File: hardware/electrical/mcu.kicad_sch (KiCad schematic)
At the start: 45 parts, among them J2 STDC14, SW1 SW_Push, SW2 SW_SPST, U2 STM32F446ZET6, U3 SRV05-4, Y1 X322516MLB4SI, Y2 Q13FC1350000400

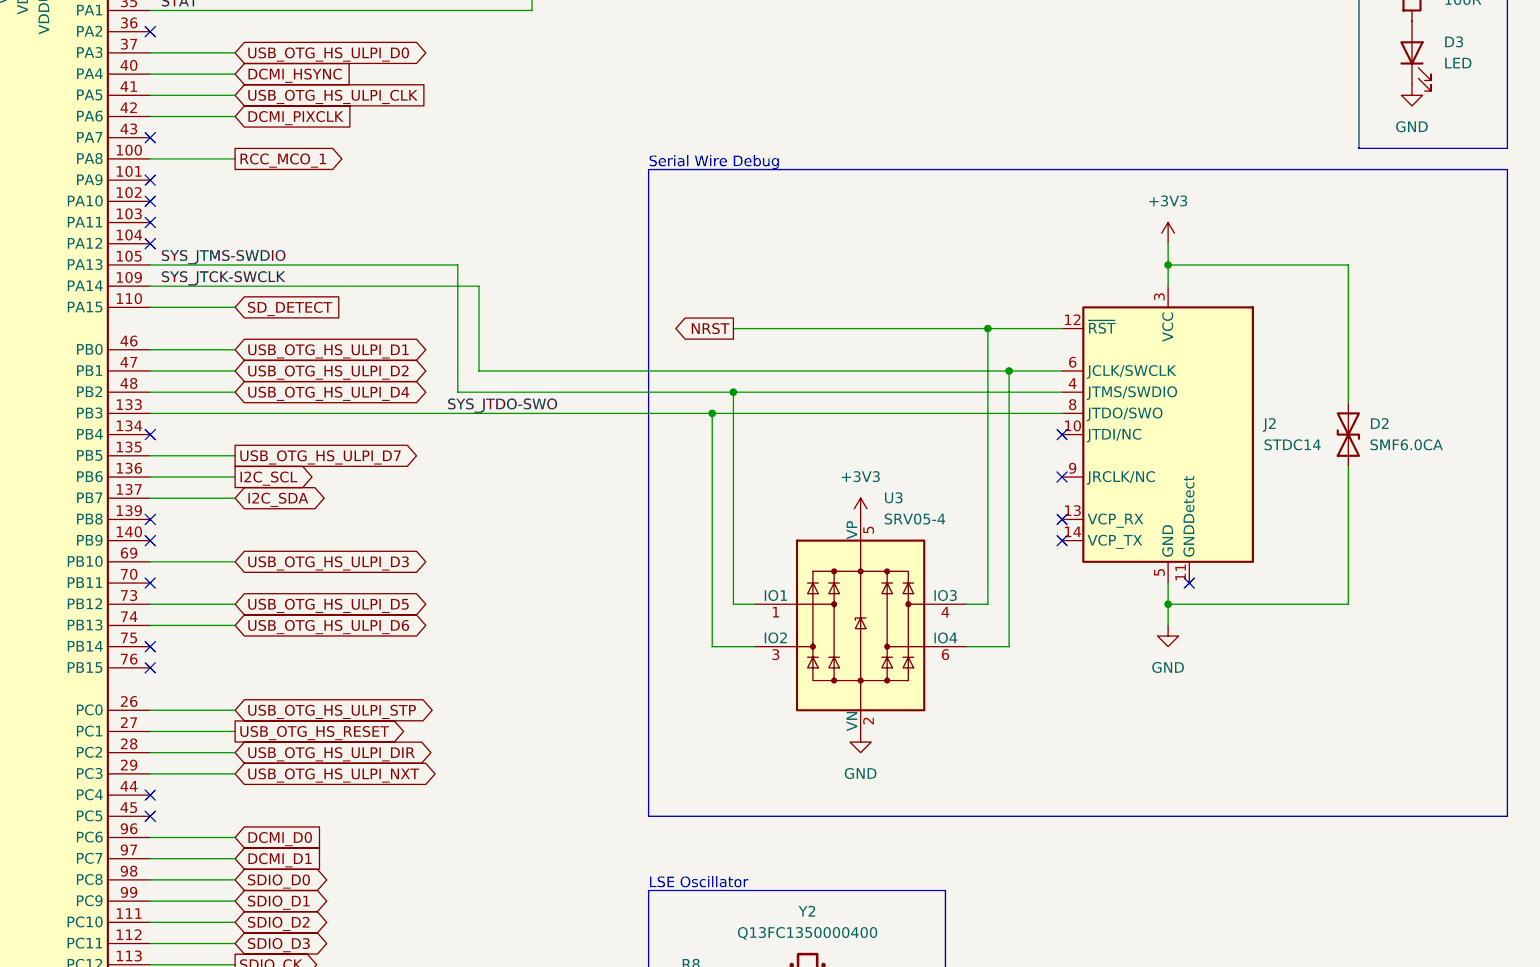
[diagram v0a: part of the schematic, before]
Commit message: Remove ESD protection from SWD connector
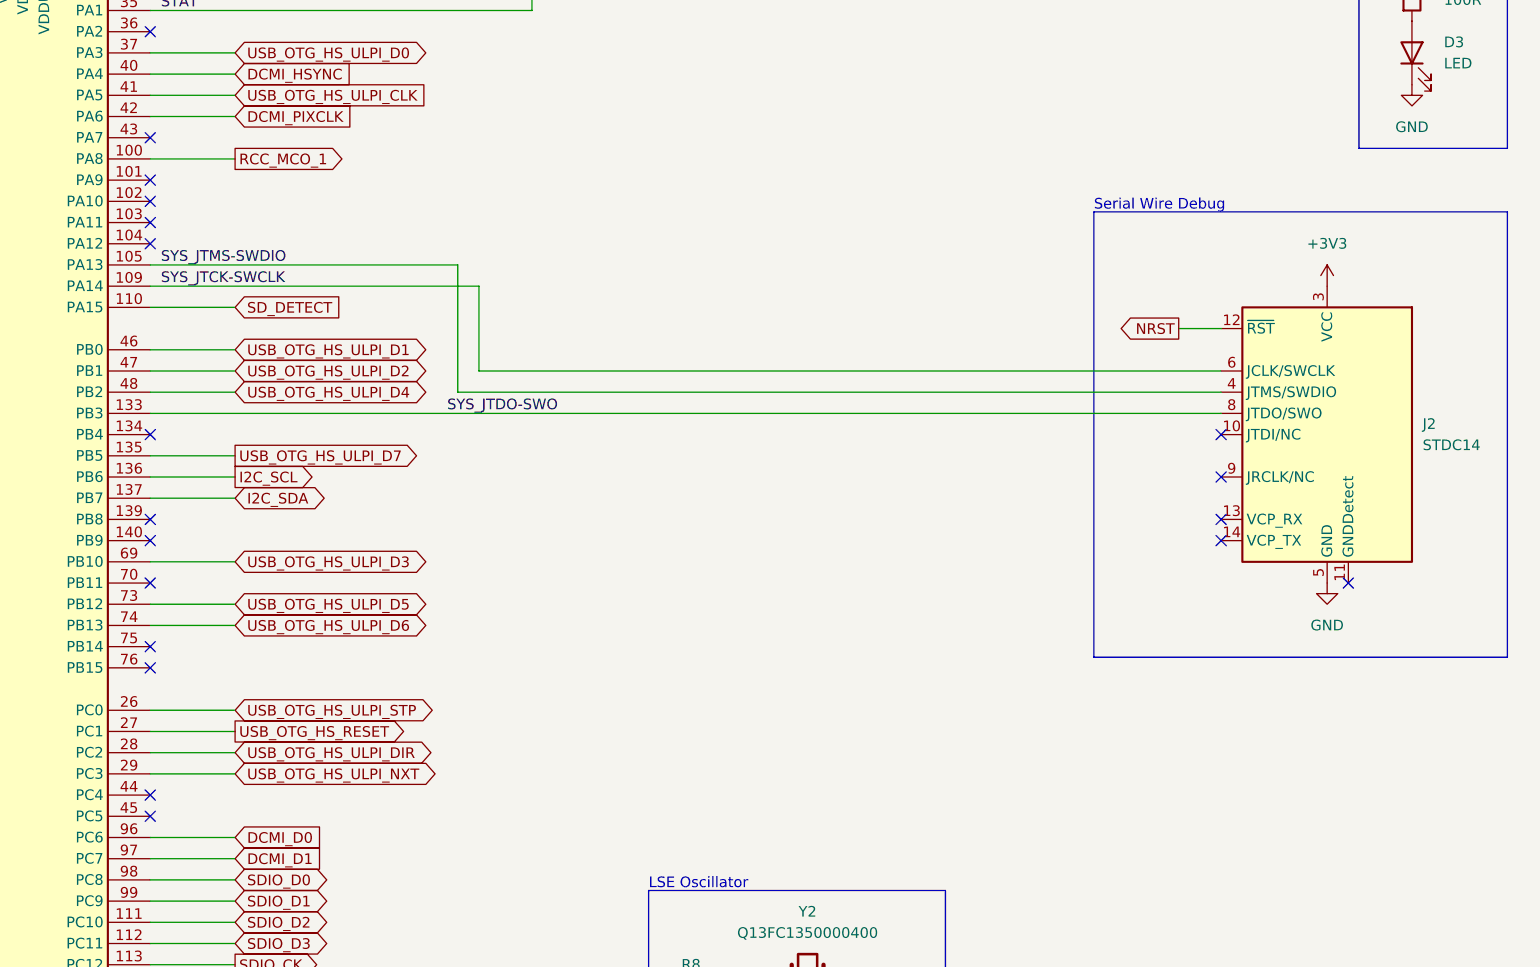
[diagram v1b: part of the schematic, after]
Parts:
- removed D2: SMF6.0CA, symbol Device:D_TVS
- removed U3: SRV05-4, Package_TO_SOT_SMD:SOT-23-6, symbol Power_Protection:SRV05-4
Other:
- moved on the sheet: J2

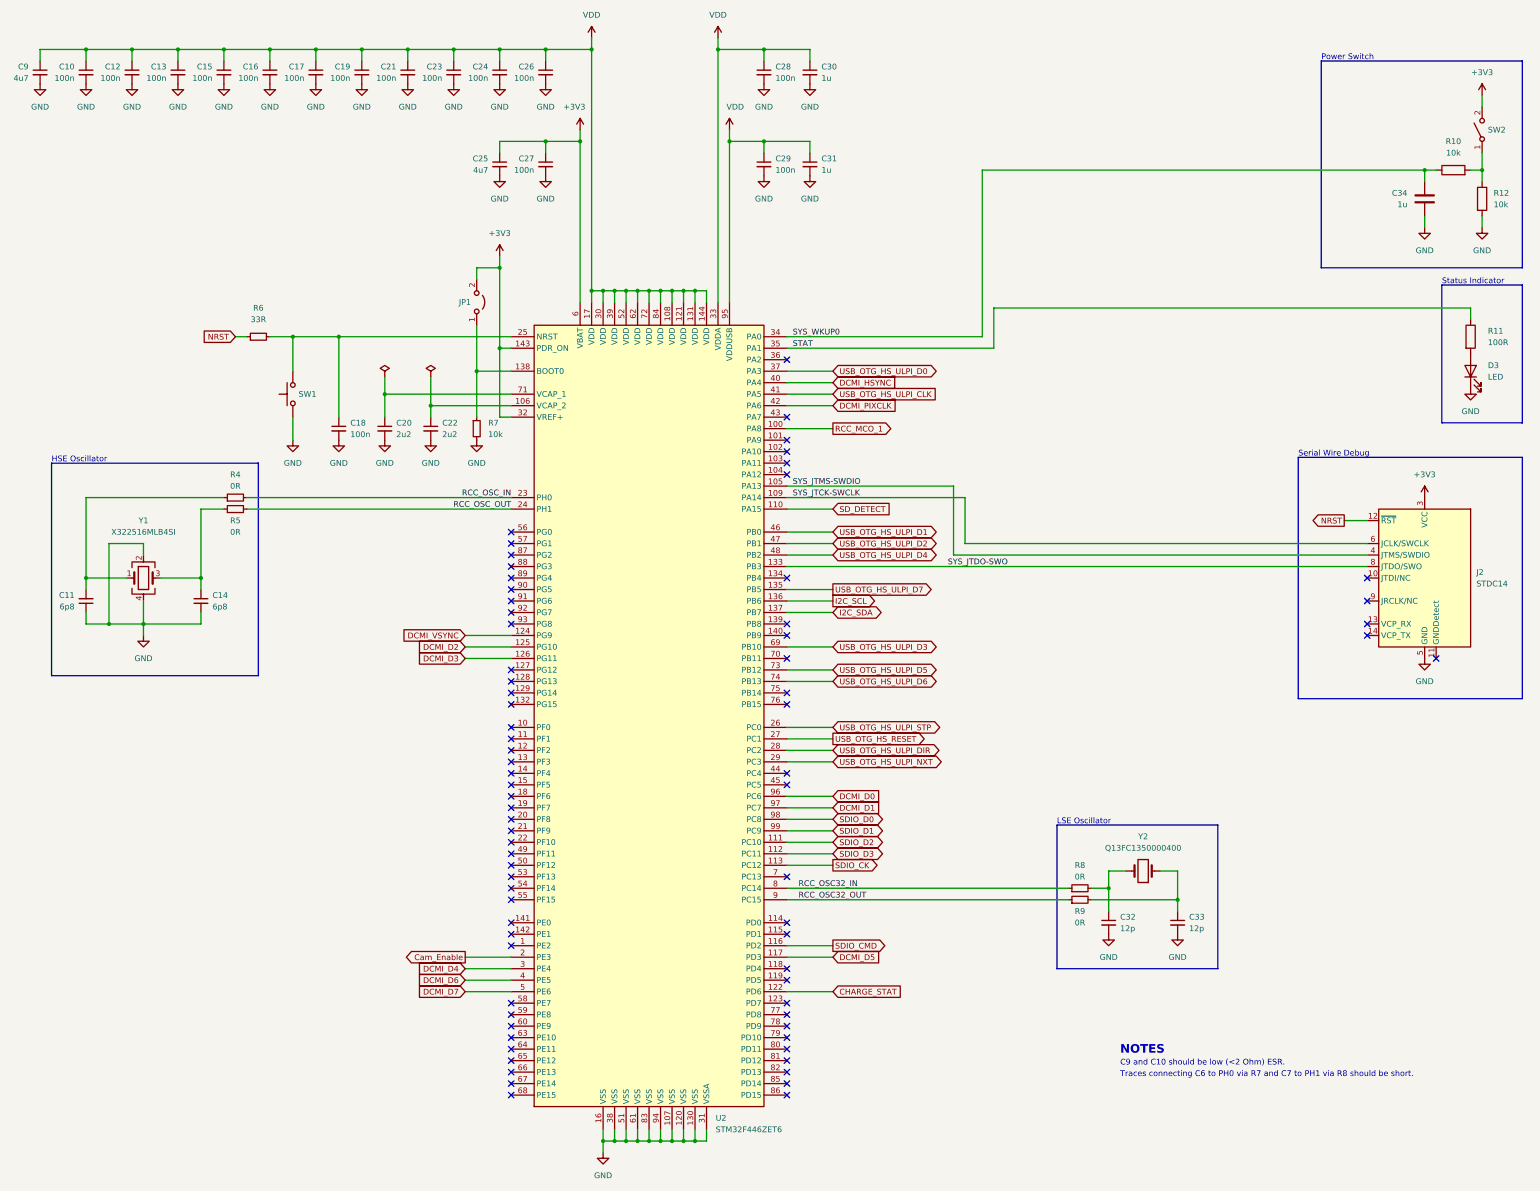
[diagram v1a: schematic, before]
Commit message: Update footprints to KiCad 7.0 versions
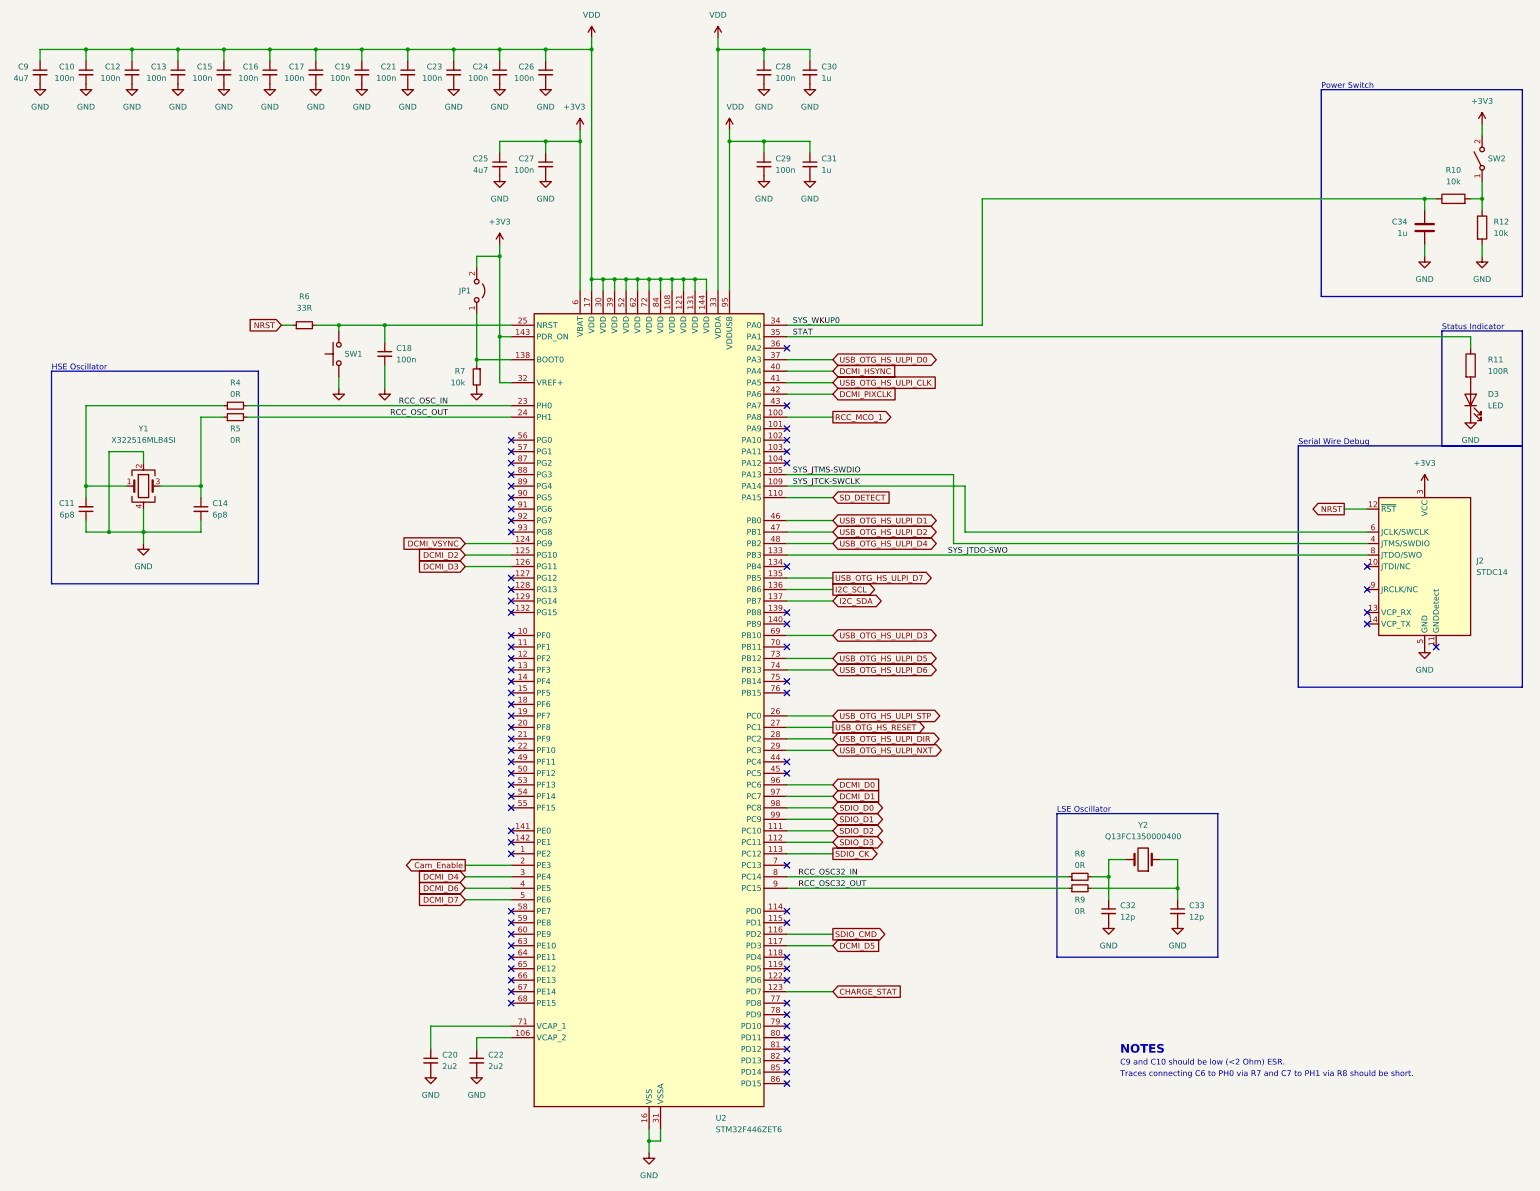
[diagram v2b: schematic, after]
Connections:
- net CHARGE_STAT: now also U2.123 (PD7); no longer U2.122 (PD6)
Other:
- moved on the sheet: C11, C14, C18, C20, C22, C32, C33, C34, D3, J2, JP1, R10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

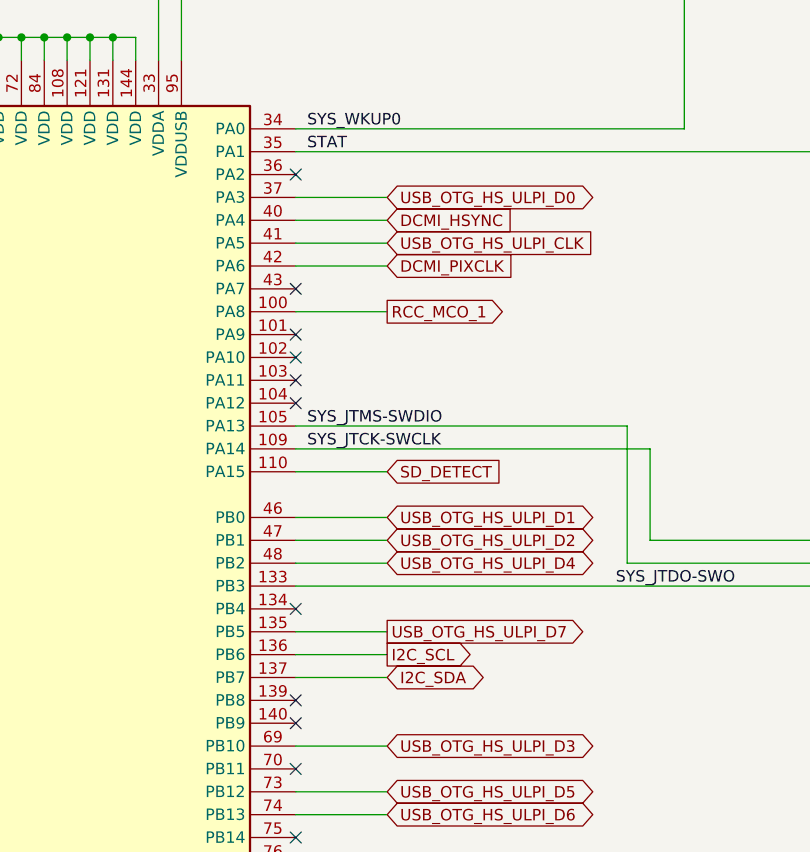
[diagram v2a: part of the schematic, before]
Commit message: Update camera connector schematic * Connect PWDN and PCLK to MCU * Replace SG-210STF (2520) with SG-8018CA (7050) * Mark X2 and C54 as DNP * Replace regulators with TLV700*
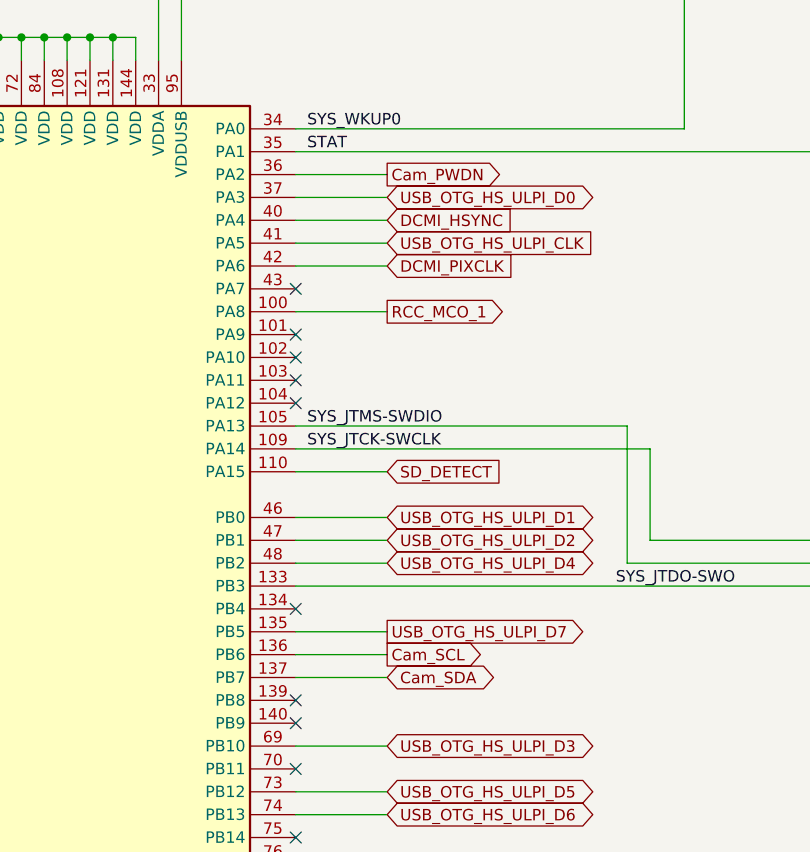
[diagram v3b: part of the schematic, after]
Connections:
- net Cam_PWDN: now reaches U2.36 (PA2)
- net I2C_SCL renamed Cam_SCL
- net I2C_SDA renamed Cam_SDA
- no-connect marks 74 -> 73
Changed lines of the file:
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@@
   (no_connect (at 226.06 149.86))
   (no_connect (at 226.06 215.9))
-  (no_connect (at 226.06 91.44))
   (no_connect (at 226.06 254))
   (no_connect (at 165.1 144.78))
@@
     (stroke (width 0) (type default))
   )
+  (wire (pts (xy 226.06 91.44) (xy 236.22 91.44))
+    (stroke (width 0) (type default))
+  )
   (wire (pts (xy 101.6 25.4) (xy 91.44 25.4))
     (stroke (width 0) (type default))
@@
     )
   )
-  (global_label "I2C_SCL" (shape output) (at 236.22 144.78 0) (fields_autoplaced)
-    (effects (font (size 1.27 1.27)) (justify left))
-    (property "Intersheetrefs" "${INTERSHEET_REFS}" (at 246.1926 144.7006 0)
+  (global_label "Cam_SCL" (shape output) (at 236.22 144.78 0) (fields_autoplaced)
+    (effects (font (size 1.27 1.27)) (justify left))
+    (property "Intersheetrefs" "${INTERSHEET_REFS}" (at 247.7133 144.78 0)
       (effects (font (size 1.27 1.27)) (justify left) hide)
     )
@@
     )
   )
-  (global_label "I2C_SDA" (shape bidirectional) (at 236.22 147.32 0) (fields_autoplaced)
-    (effects (font (size 1.27 1.27)) (justify left))
-    (property "Intersheetrefs" "${INTERSHEET_REFS}" (at 246.2531 147.2406 0)
+  (global_label "Cam_SDA" (shape bidirectional) (at 236.22 147.32 0) (fields_autoplaced)
+    (effects (font (size 1.27 1.27)) (justify left))
+    (property "Intersheetrefs" "${INTERSHEET_REFS}" (at 248.8851 147.32 0)
       (effects (font (size 1.27 1.27)) (justify left) hide)
     )
@@
       (effects (font (size 1.27 1.27)) (justify left) hide)
     )
+  )
+  (global_label "Cam_PWDN" (shape output) (at 236.22 91.44 0) (fields_autoplaced)
+    (effects (font (size 1.27 1.27)) (justify left))
+    (property "Intersheetrefs" "${INTERSHEET_REFS}" (at 249.5276 91.44 0)
+      (effects (font (size 1.27 1.27)) (justify left) hide)
+    )
